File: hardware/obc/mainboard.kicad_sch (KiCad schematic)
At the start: 0 parts

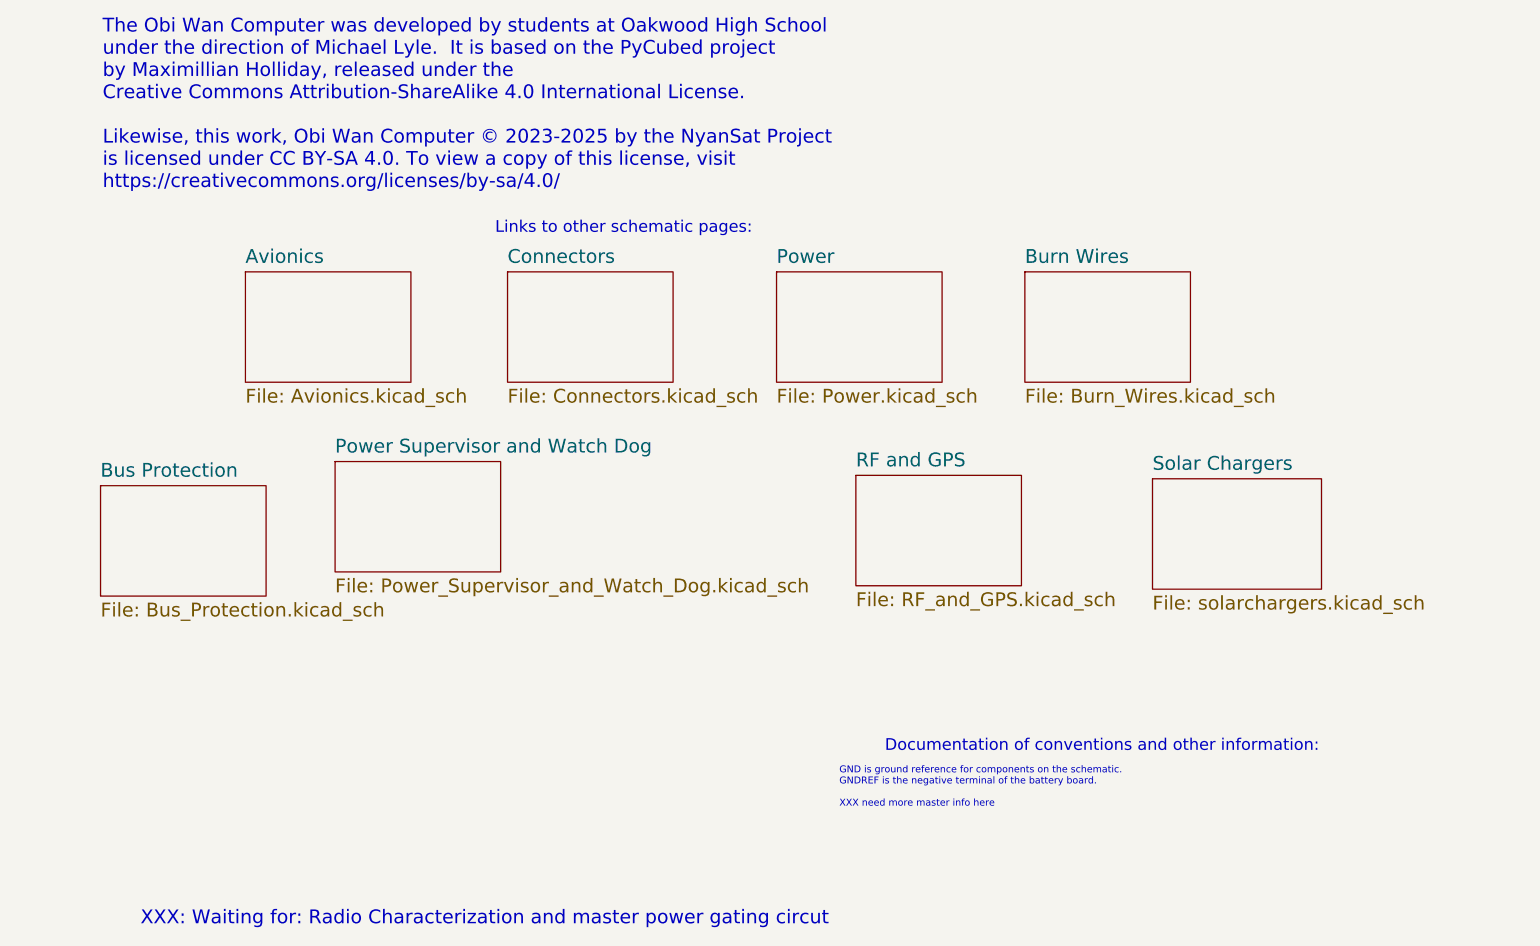
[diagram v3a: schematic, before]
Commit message: obc: changed flash memory to PSRAM
- Fixed MRAM symbol
- Removed Flash memory for new PSRAM
- Changed labels on Avionics page to match format
- Added another 0.1uF capacitor to VRAG pins
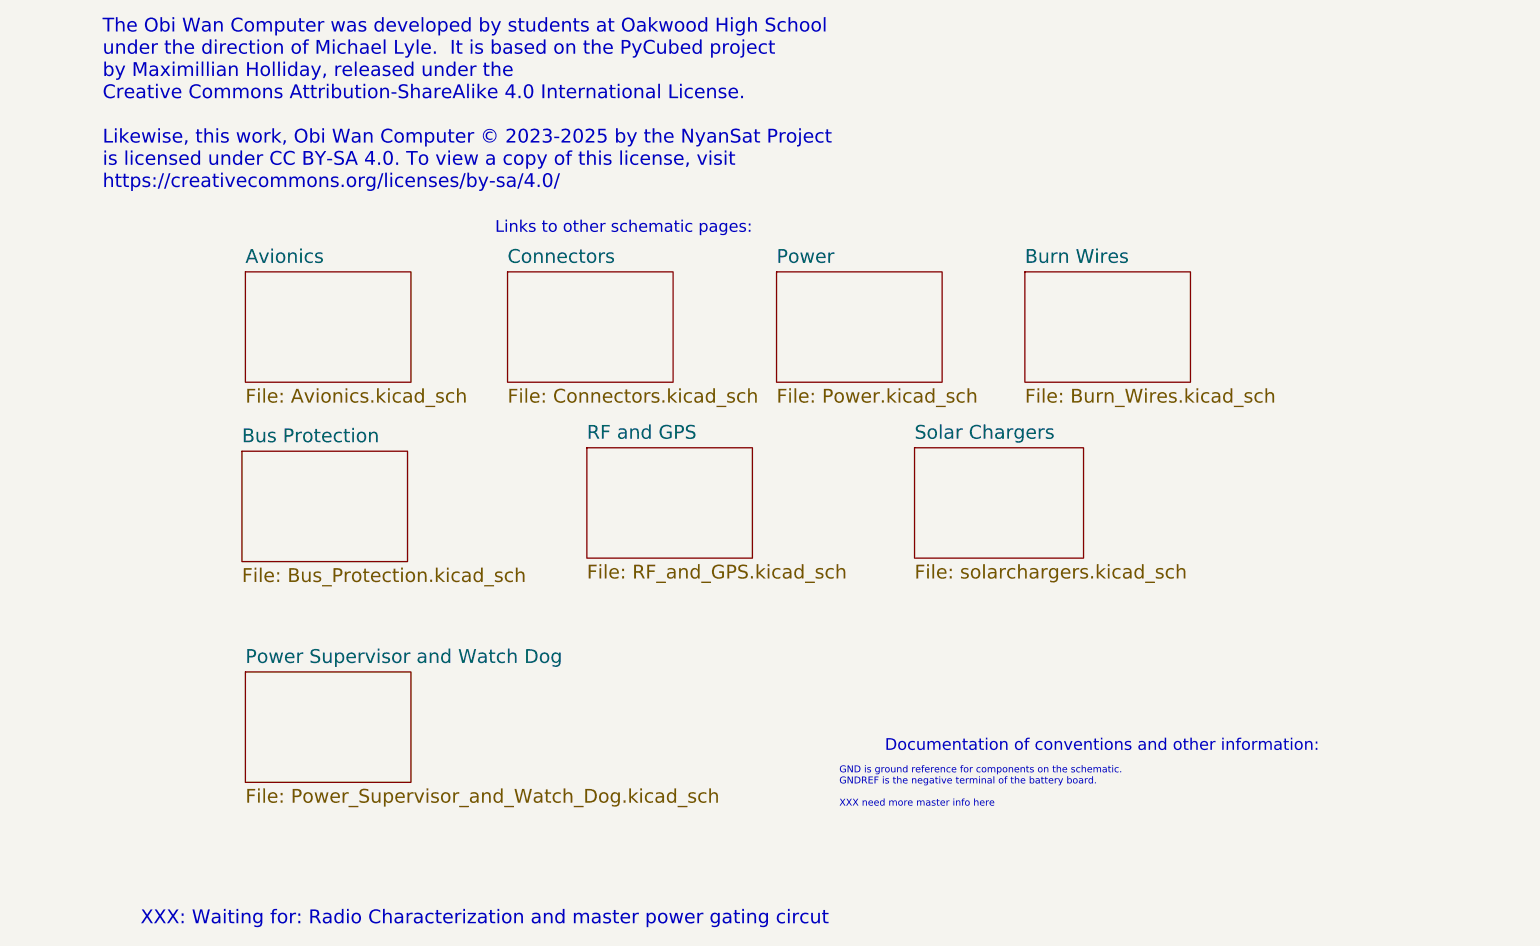
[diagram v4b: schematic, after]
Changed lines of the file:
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@@
 	)
 	(sheet
-		(at 156.21 100.33)
+		(at 106.68 95.25)
 		(size 30.48 20.32)
 		(fields_autoplaced yes)
@@
 		)
 		(property "Sheetname" "RF and GPS"
-			(at 156.21 98.9834 0)
+			(at 106.68 93.9034 0)
 			(effects
 				(font
@@
 		)
 		(property "Sheetfile" "RF_and_GPS.kicad_sch"
-			(at 156.21 121.7426 0)
+			(at 106.68 116.6626 0)
 			(effects
 				(font
@@
 	)
 	(sheet
-		(at 17.145 102.235)
+		(at 43.18 95.885)
 		(size 30.48 20.32)
 		(fields_autoplaced yes)
@@
 		)
 		(property "Sheetname" "Bus Protection"
-			(at 17.145 100.8884 0)
+			(at 43.18 94.5384 0)
 			(effects
 				(font
@@
 		)
 		(property "Sheetfile" "Bus_Protection.kicad_sch"
-			(at 17.145 123.6476 0)
+			(at 43.18 117.2976 0)
 			(effects
 				(font
@@
 	)
 	(sheet
-		(at 60.325 97.79)
+		(at 43.815 136.525)
 		(size 30.48 20.32)
 		(fields_autoplaced yes)
@@
 		)
 		(property "Sheetname" "Power Supervisor and Watch Dog"
-			(at 60.325 96.4434 0)
+			(at 43.815 135.1784 0)
 			(effects
 				(font
@@
 		)
 		(property "Sheetfile" "Power_Supervisor_and_Watch_Dog.kicad_sch"
-			(at 60.325 119.2026 0)
+			(at 43.815 157.9376 0)
 			(effects
 				(font
@@
 	)
 	(sheet
-		(at 210.82 100.965)
+		(at 167.005 95.25)
 		(size 31.115 20.32)
 		(fields_autoplaced yes)
@@
 		)
 		(property "Sheetname" "Solar Chargers"
-			(at 210.82 99.6184 0)
+			(at 167.005 93.9034 0)
 			(effects
 				(font
@@
 		)
 		(property "Sheetfile" "solarchargers.kicad_sch"
-			(at 210.82 122.3776 0)
+			(at 167.005 116.6626 0)
 			(effects
 				(font

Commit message: obc: Fixed errors from design review
- Gave proper attribution on all pages
- Spread out components on Avionics page
- Changed GPS power circuit
- Added a DNP resistor in between VBATT and VWATCHEDRAIL
- Added various other part numbers on Power Supervisor and Watch Dog Page
- Changed Power Supervisor and Watch Dog Page to page 3
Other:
- company: Ruchir Kavulli, Michael Lyle -> Ruchir Kavulli, Luke Titi, Michael Lyle
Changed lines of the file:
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@@
 		(date "2024-06-07")
 		(rev "1")
-		(company "Ruchir Kavulli, Michael Lyle")
+		(company "Ruchir Kavulli, Luke Titi, Michael Lyle")
 		(comment 1 "Derived from PyCubed Mainboard v5")
 	)
@@
 			(project "mainboard"
 				(path "/e3ac22ea-6806-4807-a025-571315789c25"
-					(page "5")
+					(page "6")
 				)
 			)
@@
 			(project "mainboard"
 				(path "/e3ac22ea-6806-4807-a025-571315789c25"
-					(page "4")
+					(page "5")
 				)
 			)
@@
 			(project "mainboard"
 				(path "/e3ac22ea-6806-4807-a025-571315789c25"
-					(page "7")
+					(page "8")
 				)
 			)
@@
 			(project "mainboard"
 				(path "/e3ac22ea-6806-4807-a025-571315789c25"
-					(page "6")
+					(page "7")
 				)
 			)
@@
 			(project "mainboard"
 				(path "/e3ac22ea-6806-4807-a025-571315789c25"
-					(page "3")
+					(page "4")
 				)
 			)
@@
 			(project "mainboard"
 				(path "/e3ac22ea-6806-4807-a025-571315789c25"
-					(page "9")
+					(page "3")
 				)
 			)
@@
 			(project "mainboard"
 				(path "/e3ac22ea-6806-4807-a025-571315789c25"
-					(page "8")
-				)
-			)
+					(page "9")
+				)
+			)

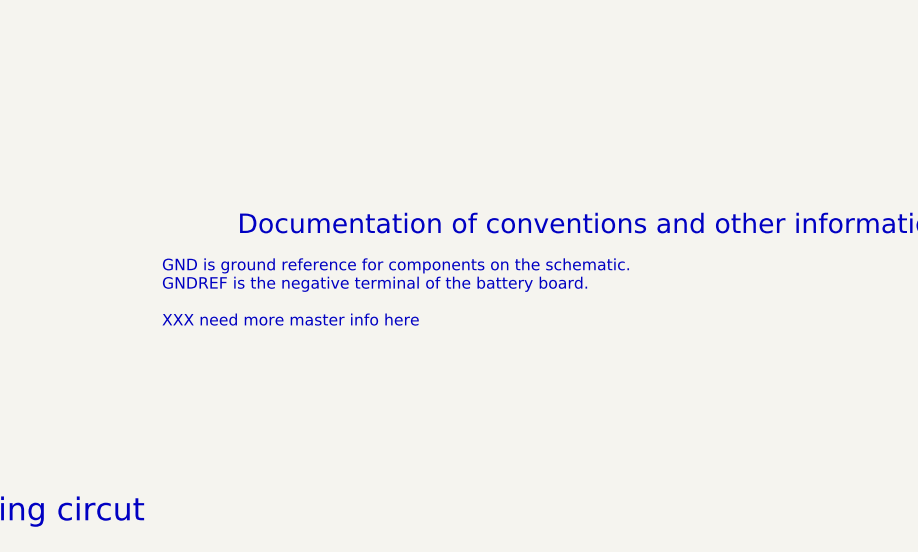
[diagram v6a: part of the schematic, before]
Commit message: obc: additional gndref -> packneg
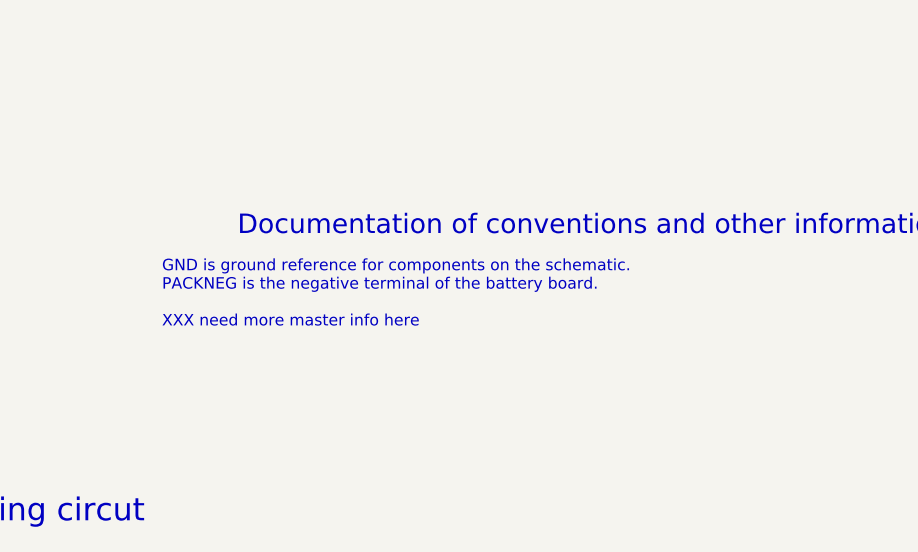
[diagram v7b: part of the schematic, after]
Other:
- note added: "GND is ground reference for components on the schematic. PACKNEG is the negative terminal of the battery board. XXX need more master info here"
- note removed: "GND is ground reference for components on the schematic. GNDREF is the negative terminal of the battery board. XXX need more master info here"
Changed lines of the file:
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@@
 		)
 	)
-	(text "GND is ground reference for components on the schematic. \nGNDREF is the negative terminal of the battery board.\n\nXXX need more master info here"
+	(text "GND is ground reference for components on the schematic. \nPACKNEG is the negative terminal of the battery board.\n\nXXX need more master info here"
 		(exclude_from_sim no)
 		(at 153.162 157.734 0)
